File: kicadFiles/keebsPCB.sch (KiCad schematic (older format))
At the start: 165 parts, among them J1 TYPE-C-31-M12_13, J2 Conn_ARM_JTAG_SWD_10, J3 Conn_01x14, J4 Conn_01x14, SW1 ESC, SW10 9, SW11 0, SW12 -_, SW13 =+, SW14 BKSP_200, SW15 TAB_150, SW16 Q, SW17 W, SW18 E, SW19 R, SW2 1, SW20 T, SW21 Y, SW22 U, SW23 I, SW24 L, SW25 O, SW26 P, SW27 [{, SW28 ]}, SW29 CAPS_175, SW3 2, SW30 A, SW31 S, SW32 D, SW33 F, SW34 G, SW35 H, SW36 J, SW37 K, SW38 L, SW39 :;, SW4 3, SW40 \", SW41 ENTER_225, SW42 LSHIFT_225, SW43 Z, SW44 X, SW45 C, SW46 V, SW47 B, SW48 N, SW49 M, SW5 4, SW50 <,, SW51 .>, SW52 ?/, SW53 RSHIFT_275, SW54 MXSwitch, SW55 MXSwitch, SW56 MXSwitch, SW57 MXSwitch, SW58 MXSwitch, SW59 MXSwitch, SW6 5, SW60 MXSwitch, SW7 6, SW8 7, SW9 8, U1 STM32F072-LQFP48, U2 USBLC6-2SC6, U3 MCP1700-3302E_SOT23

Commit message: iso done
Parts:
- removed D1, D10, D11, D12, D13, D14, D15, D16, D17, D18, D19, D2, D20, D21, D22, D23, D24, D25, D26, D27, D28, D29, D3, D30, D31, D32, D33, D34, D35, D36, D37, D38, D39, D4, D40, D41, D42, D43, D44, D45, D46, D47, D48, D49, D5, D50, D51, D52, D53, D54, D55, D56, D57, D58, D59, D6, D60, D7, D8, D9: 1N4148, acheron_Components:D_SOD-123, symbol Device:D
- removed J3: Conn_01x14, acheron_Connectors:PinHeader_1x7_P2.54mm_Vertical, symbol Connector_Generic:Conn_01x07
- removed J4: Conn_01x14, acheron_Connectors:PinHeader_1x8_P2.54mm_Vertical, symbol Connector_Generic:Conn_01x08
- removed L1: Keebs Logo, keebsLogo:keebsLogo, symbol Mechanical:MountingHole
- removed L2: OSHLogo, oshLogo:osh-logo, symbol Mechanical:MountingHole
- removed L3: Keebs Label, keebsLogo:keebsLabel, symbol Mechanical:MountingHole
- removed L4: Keebs Label Mask, keebsLogo:keebsLabelMask, symbol Mechanical:MountingHole
- added D1, D10, D11, D12, D13, D14, D15, D16, D17, D18, D19, D2, D20, D21, D22, D23, D24, D25, D26, D27, D28, D29, D3, D30, D31, D32, D33, D34, D35, D36, D37, D38, D39, D4, D40, D41, D42, D43, D44, D45, D46, D47, D48, D49, D5, D50, D51, D52, D53, D54, D55, D56, D57, D58, D59, D6, D60, D61, D62, D7, D8, D9: 1N4148, acheron_Components:D_SOD-123, symbol Device:D_Small
- added SW61: RCTRL_125, acheron_MX:MX125H, symbol acheronSymbols:MXSwitch
- added SW62: KC_NUBS, acheron_MX:MX100H, symbol acheronSymbols:MXSwitch
- SW14: value BKSP_200 -> BCKSPC_200
- SW24: value L -> O
- SW25: value O -> P
- SW26: value P -> [{
- SW27: value [{ -> ]}
- SW28: value ]} -> KC_NUHS; footprint acheron_MX:MX150H -> acheron_MX:MX100H
- SW29: value CAPS_175 -> CAPSLOCK_175
- SW39: value :; -> ;:
- SW40: value \" -> '\"
- SW41: value ENTER_225 -> ENTER_ISO; footprint acheron_MX:MX225H -> acheron_MX:MX_ISOEnter_Vertical
- SW42: value LSHIFT_225 -> LSHIFT_125; footprint acheron_MX:MX225H -> acheron_MX:MX125H
- SW50: value <, -> ,<
- SW52: value ?/ -> /?
- SW54: value MXSwitch -> LCTRL_125; footprint acheron_MX:MX150H -> acheron_MX:MX125H
- SW55: value MXSwitch -> LGUI_125; footprint acheron_MX:MX100H -> acheron_MX:MX125H
- SW56: value MXSwitch -> LALT_125; footprint acheron_MX:MX150H -> acheron_MX:MX125H
- SW57: value MXSwitch -> SPACE_625; footprint acheron_MX:MX700HR -> acheron_MX:MX625HR
- SW58: value MXSwitch -> RALT_125; footprint acheron_MX:MX150H -> acheron_MX:MX125H
- SW59: value MXSwitch -> RGUI_125; footprint acheron_MX:MX100H -> acheron_MX:MX125H
- SW60: value MXSwitch -> FN_125; footprint acheron_MX:MX150H -> acheron_MX:MX125H
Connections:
- net labels added: Col14
- net labels removed: Extra1, Extra10, Extra11, Extra12, Extra13, Extra14, Extra15, Extra2, Extra3, Extra4, Extra5, Extra6, Extra7, Extra8, Extra9
- wire segments 348 -> 338
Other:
- note removed: "Extra pins"
- note removed: "Logos and flags"
- note removed: "Switch matrix"

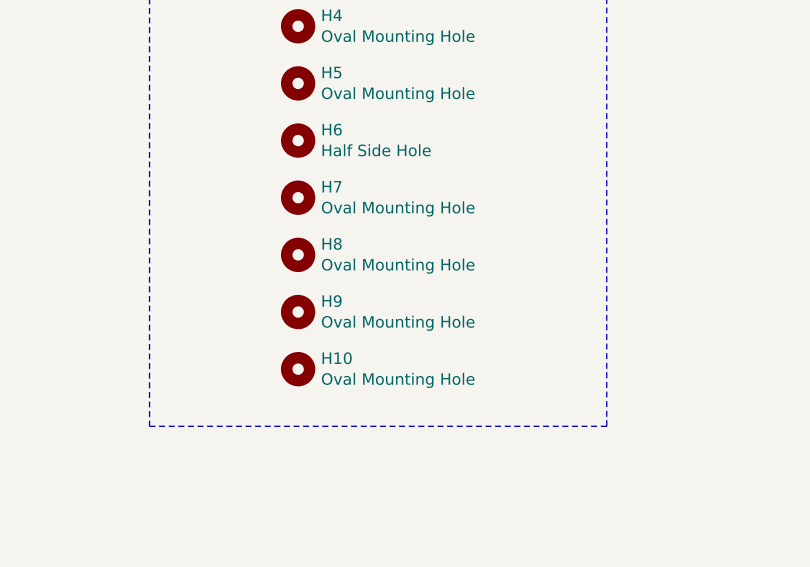
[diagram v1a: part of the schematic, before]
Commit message: removing extra holes
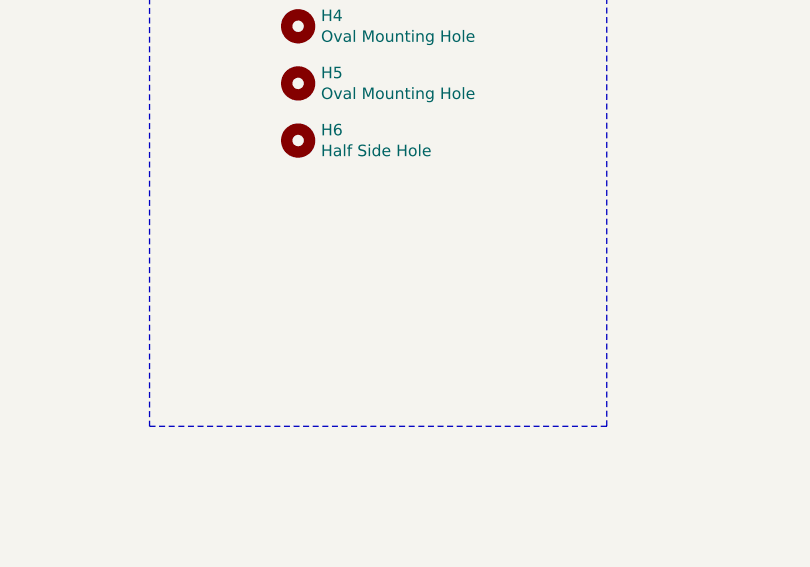
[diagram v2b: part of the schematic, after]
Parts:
- removed H10, H8: Oval Mounting Hole, acheron_MountingHoles:MoutingHole_Oval_BackOnly_7mm_5.0x2.5mm, symbol Mechanical:MountingHole
- removed H7, H9: Oval Mounting Hole, acheron_MountingHoles:MoutingHole_Oval_7mm_5.0x2.5mm, symbol Mechanical:MountingHole
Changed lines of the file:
@@
-	1    0    0    -1
-$EndComp
-$Comp
-L Mechanical:MountingHole H7
-U 1 1 5E63D297
-P 4800 18975
-F 0 "H7" H 4900 19021 50  0000 L CNN
-F 1 "Oval Mounting Hole" H 4900 18930 50  0000 L CNN
-F 2 "acheron_MountingHoles:MoutingHole_Oval_7mm_5.0x2.5mm" H 4800 18975 50  0001 C CNN
-F 3 "~" H 4800 18975 50  0001 C CNN
-	1    4800 18975
-	1    0    0    -1
-$EndComp
-$Comp
-L Mechanical:MountingHole H8
-U 1 1 5E63D4E1
-P 4800 19225
-F 0 "H8" H 4900 19271 50  0000 L CNN
-F 1 "Oval Mounting Hole" H 4900 19180 50  0000 L CNN
-F 2 "acheron_MountingHoles:MoutingHole_Oval_BackOnly_7mm_5.0x2.5mm" H 4800 19225 50  0001 C CNN
-F 3 "~" H 4800 19225 50  0001 C CNN
-	1    4800 19225
-	1    0    0    -1
-$EndComp
-$Comp
-L Mechanical:MountingHole H9
-U 1 1 5E63D910
-P 4800 19475
-F 0 "H9" H 4900 19521 50  0000 L CNN
-F 1 "Oval Mounting Hole" H 4900 19430 50  0000 L CNN
-F 2 "acheron_MountingHoles:MoutingHole_Oval_7mm_5.0x2.5mm" H 4800 19475 50  0001 C CNN
-F 3 "~" H 4800 19475 50  0001 C CNN
-	1    4800 19475
-	1    0    0    -1
-$EndComp
-$Comp
-L Mechanical:MountingHole H10
-U 1 1 5E64C744
-P 4800 19725
-F 0 "H10" H 4900 19771 50  0000 L CNN
-F 1 "Oval Mounting Hole" H 4900 19680 50  0000 L CNN
-F 2 "acheron_MountingHoles:MoutingHole_Oval_BackOnly_7mm_5.0x2.5mm" H 4800 19725 50  0001 C CNN
-F 3 "~" H 4800 19725 50  0001 C CNN
-	1    4800 19725
 	1    0    0    -1
 $EndComp

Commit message: first plate attempt
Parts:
- removed CB1: 1uF, Capacitor_SMD:C_0402_1005Metric, symbol Device:C_Small
- removed CB2: 10n, Capacitor_SMD:C_0402_1005Metric, symbol Device:C_Small
- removed CB3, CB5, CB8, CUSB1: 100n, Capacitor_SMD:C_0402_1005Metric, symbol Device:C_Small
- removed CB4, CB6: 4.7uF, Capacitor_SMD:C_0402_1005Metric, symbol Device:C_Small
- removed CB7: 100nF, Capacitor_SMD:C_0402_1005Metric, symbol Device:C_Small
- removed CRST1, CSI1: 10u, Capacitor_SMD:C_0805_2012Metric_Pad1.15x1.40mm_HandSolder, symbol Device:C_Small
- removed CRST2: 4.7n, Capacitor_SMD:C_0805_2012Metric_Pad1.15x1.40mm_HandSolder, symbol Device:C_Small
- removed CSH1: 4.7nF, Capacitor_SMD:C_0805_2012Metric, symbol Device:C_Small
- removed CSO1: 1u, Capacitor_SMD:C_0805_2012Metric_Pad1.15x1.40mm_HandSolder, symbol Device:C_Small
- removed DF1: RB060M-60TR, acheron_Components:D_SOD-123, symbol Device:D_Schottky
- removed DRST1, DS1: 1N4148, acheron_Components:D_SOD-123, symbol Device:D
- removed F1: Polyfuse, acheron_Components:Fuse_1812_4532, symbol Device:Polyfuse_Small
- removed H1, H6: Half Side Hole, acheron_MountingHoles:halfSideHole, symbol Mechanical:MountingHole
- removed H2: Mounting Hole, acheron_MountingHoles:MoutingHole_Oval_7mm_5.0x2.5mm, symbol Mechanical:MountingHole
- removed H3, H5: Oval Mounting Hole, acheron_MountingHoles:MoutingHole_Oval_BackOnly_7mm_5.0x2.5mm, symbol Mechanical:MountingHole
- removed H4: Oval Mounting Hole, acheron_MountingHoles:MoutingHole_Oval_7mm_5.0x2.5mm, symbol Mechanical:MountingHole
- removed J1: TYPE-C-31-M12_13, acheron_Connectors:TYPE-C-31-M-12, symbol acheronSymbols:TYPE-C-31-M12_13
- removed J2: Conn_ARM_JTAG_SWD_10, acheron_Connectors:Conn_ARM_JTAG_SWD_10, symbol Connector:Conn_ARM_JTAG_SWD_10
- removed QRST1: DTC123J, Package_TO_SOT_SMD:SOT-23, symbol Transistor_BJT:DTC123J
- removed RCC1, RCC2: 5.1k, Resistor_SMD:R_0402_1005Metric, symbol Device:R_Small
- removed RRST1: 100k, acheron_Components:R_SMD_1026, symbol Device:R_Small
- removed RSH1: 1M, acheron_Components:R_SMD_1026, symbol Device:R_Small
- removed SWRST1: SW_Push, acheron_Hardware:smdPushBtn, symbol Switch:SW_Push
- removed U1: STM32F072-LQFP48, acheron_Components:LQFP-48_7x7mm_P0.5mm, symbol acheronSymbols:STM32F072-LQFP48
- removed U2: USBLC6-2SC6, acheron_Components:SOT-23-6, symbol Power_Protection:USBLC6-2SC6
- removed U3: MCP1700-3302E_SOT23, Package_TO_SOT_SMD:SOT-23, symbol Regulator_Linear:MCP1700-3302E_SOT23
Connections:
- net labels added: tierra
- net labels removed: 3.3V, 5V, BOOT0, Col1, Col10, Col11, Col12, Col13, Col14, Col2, Col3, Col4, Col5, Col6, Col7, Col8, Col9, D+, D-, DBus+, DBus-, GND, NRST, Row1, Row2, Row3, Row4, Row5, SHIELD, SWCLK, SWDIO, VBUS
- wire segments 338 -> 195
- no-connect marks 4 -> 0
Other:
- note removed: "CBx are the bypass capacitors. Their value is specified in reference [2]."
- note removed: "Hard reset circuit"
- note removed: "MCU"
- note removed: "Mounting holes"
- note removed: "Power supply and protection circuit"
- note removed: "SWD"
- note removed: "Shield"
- note removed: "USB Connector"
- note removed: "USD ESD"

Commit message: reset
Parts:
- removed D1, D10, D11, D12, D13, D14, D15, D16, D17, D18, D19, D2, D20, D21, D22, D23, D24, D25, D26, D27, D28, D29, D3, D30, D31, D32, D33, D34, D35, D36, D37, D38, D39, D4, D40, D41, D42, D43, D44, D45, D46, D47, D48, D49, D5, D50, D51, D52, D53, D54, D55, D56, D57, D58, D59, D6, D60, D61, D62, D7, D8, D9: 1N4148, acheron_Components:D_SOD-123, symbol Device:D_Small
- removed SW61: RCTRL_125, acheron_MX:MX125H, symbol acheronSymbols:MXSwitch
- removed SW62: KC_NUBS, acheron_MX:MX100H, symbol acheronSymbols:MXSwitch
- added CB1: 1uF, Capacitor_SMD:C_0402_1005Metric, symbol Device:C_Small
- added CB2: 10n, Capacitor_SMD:C_0402_1005Metric, symbol Device:C_Small
- added CB3, CB5, CB8, CUSB1: 100n, Capacitor_SMD:C_0402_1005Metric, symbol Device:C_Small
- added CB4, CB6: 4.7uF, Capacitor_SMD:C_0402_1005Metric, symbol Device:C_Small
- added CB7: 100nF, Capacitor_SMD:C_0402_1005Metric, symbol Device:C_Small
- added CRST1, CSI1: 10u, Capacitor_SMD:C_0805_2012Metric_Pad1.15x1.40mm_HandSolder, symbol Device:C_Small
- added CRST2: 4.7n, Capacitor_SMD:C_0805_2012Metric_Pad1.15x1.40mm_HandSolder, symbol Device:C_Small
- added CSH1: 4.7nF, Capacitor_SMD:C_0805_2012Metric, symbol Device:C_Small
- added CSO1: 1u, Capacitor_SMD:C_0805_2012Metric_Pad1.15x1.40mm_HandSolder, symbol Device:C_Small
- added D1, D10, D11, D12, D13, D14, D15, D16, D17, D18, D19, D2, D20, D21, D22, D23, D24, D25, D26, D27, D28, D29, D3, D30, D31, D32, D33, D34, D35, D36, D37, D38, D39, D4, D40, D41, D42, D43, D44, D45, D46, D47, D48, D49, D5, D50, D51, D52, D53, D54, D55, D56, D57, D58, D59, D6, D60, D7, D8, D9, DRST1, DS1: 1N4148, acheron_Components:D_SOD-123, symbol Device:D
- added DF1: RB060M-60TR, acheron_Components:D_SOD-123, symbol Device:D_Schottky
- added F1: Polyfuse, acheron_Components:Fuse_1812_4532, symbol Device:Polyfuse_Small
- added H1, H6: Half Side Hole, acheron_MountingHoles:halfSideHole, symbol Mechanical:MountingHole
- added H10, H3, H5, H8: Oval Mounting Hole, acheron_MountingHoles:MoutingHole_Oval_BackOnly_7mm_5.0x2.5mm, symbol Mechanical:MountingHole
- added H2: Mounting Hole, acheron_MountingHoles:MoutingHole_Oval_7mm_5.0x2.5mm, symbol Mechanical:MountingHole
- added H4, H7, H9: Oval Mounting Hole, acheron_MountingHoles:MoutingHole_Oval_7mm_5.0x2.5mm, symbol Mechanical:MountingHole
- added J1: TYPE-C-31-M12_13, acheron_Connectors:TYPE-C-31-M-12, symbol acheronSymbols:TYPE-C-31-M12_13
- added J2: Conn_ARM_JTAG_SWD_10, acheron_Connectors:Conn_ARM_JTAG_SWD_10, symbol Connector:Conn_ARM_JTAG_SWD_10
- added J3: Conn_01x14, acheron_Connectors:PinHeader_1x7_P2.54mm_Vertical, symbol Connector_Generic:Conn_01x07
- added J4: Conn_01x14, acheron_Connectors:PinHeader_1x8_P2.54mm_Vertical, symbol Connector_Generic:Conn_01x08
- added L1: Keebs Logo, keebsLogo:keebsLogo, symbol Mechanical:MountingHole
- added L2: OSHLogo, oshLogo:osh-logo, symbol Mechanical:MountingHole
- added L3: Keebs Label, keebsLogo:keebsLabel, symbol Mechanical:MountingHole
- added L4: Keebs Label Mask, keebsLogo:keebsLabelMask, symbol Mechanical:MountingHole
- added QRST1: DTC123J, Package_TO_SOT_SMD:SOT-23, symbol Transistor_BJT:DTC123J
- added RCC1, RCC2: 5.1k, Resistor_SMD:R_0402_1005Metric, symbol Device:R_Small
- added RRST1: 100k, acheron_Components:R_SMD_1026, symbol Device:R_Small
- added RSH1: 1M, acheron_Components:R_SMD_1026, symbol Device:R_Small
- added SWRST1: SW_Push, acheron_Hardware:smdPushBtn, symbol Switch:SW_Push
- added U1: STM32F072-LQFP48, acheron_Components:LQFP-48_7x7mm_P0.5mm, symbol acheronSymbols:STM32F072-LQFP48
- added U2: USBLC6-2SC6, acheron_Components:SOT-23-6, symbol Power_Protection:USBLC6-2SC6
- added U3: MCP1700-3302E_SOT23, Package_TO_SOT_SMD:SOT-23, symbol Regulator_Linear:MCP1700-3302E_SOT23
- SW14: value BCKSPC_200 -> BKSP_200
- SW24: value O -> L
- SW25: value P -> O
- SW26: value [{ -> P
- SW27: value ]} -> [{
- SW28: value KC_NUHS -> ]}; footprint acheron_MX:MX100H -> acheron_MX:MX150H
- SW29: value CAPSLOCK_175 -> CAPS_175
- SW39: value ;: -> :;
- SW40: value '\" -> \"
- SW41: value ENTER_ISO -> ENTER_225; footprint acheron_MX:MX_ISOEnter_Vertical -> acheron_MX:MX225H
- SW42: value LSHIFT_125 -> LSHIFT_225; footprint acheron_MX:MX125H -> acheron_MX:MX225H
- SW50: value ,< -> <,
- SW52: value /? -> ?/
- SW54: value LCTRL_125 -> MXSwitch; footprint acheron_MX:MX125H -> acheron_MX:MX150H
- SW55: value LGUI_125 -> MXSwitch; footprint acheron_MX:MX125H -> acheron_MX:MX100H
- SW56: value LALT_125 -> MXSwitch; footprint acheron_MX:MX125H -> acheron_MX:MX150H
- SW57: value SPACE_625 -> MXSwitch; footprint acheron_MX:MX625HR -> acheron_MX:MX700HR
- SW58: value RALT_125 -> MXSwitch; footprint acheron_MX:MX125H -> acheron_MX:MX150H
- SW59: value RGUI_125 -> MXSwitch; footprint acheron_MX:MX125H -> acheron_MX:MX100H
- SW60: value FN_125 -> MXSwitch; footprint acheron_MX:MX125H -> acheron_MX:MX150H
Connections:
- net labels added: 3.3V, 5V, BOOT0, Col1, Col10, Col11, Col12, Col13, Col2, Col3, Col4, Col5, Col6, Col7, Col8, Col9, D+, D-, DBus+, DBus-, Extra1, Extra10, Extra11, Extra12, Extra13, Extra14, Extra15, Extra2, Extra3, Extra4, Extra5, Extra6, Extra7, Extra8, Extra9, GND, NRST, Row1, Row2, Row3, Row4, Row5, SHIELD, SWCLK, SWDIO, VBUS
- net labels removed: tierra
- wire segments 195 -> 348
- no-connect marks 0 -> 4
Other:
- note added: "CBx are the bypass capacitors. Their value is specified in reference [2]."
- note added: "Extra pins"
- note added: "Hard reset circuit"
- note added: "Logos and flags"
- note added: "MCU"
- note added: "Mounting holes"
- note added: "Power supply and protection circuit"
- note added: "SWD"
- note added: "Shield"
- note added: "Switch matrix"
- note added: "USB Connector"
- note added: "USD ESD"
